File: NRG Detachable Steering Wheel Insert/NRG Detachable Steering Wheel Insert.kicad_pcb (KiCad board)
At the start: 2 copper layers, 34 x 34 mm, 18 parts, among them J1 Conn_01x01, J10 Conn_01x01, J11 Conn_01x01, J12 Conn_01x01, J13 Conn_01x01, J14 Conn_01x01, J15 Conn_01x01, J16 Conn_01x01, J2 Conn_01x01, J3 Conn_01x01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

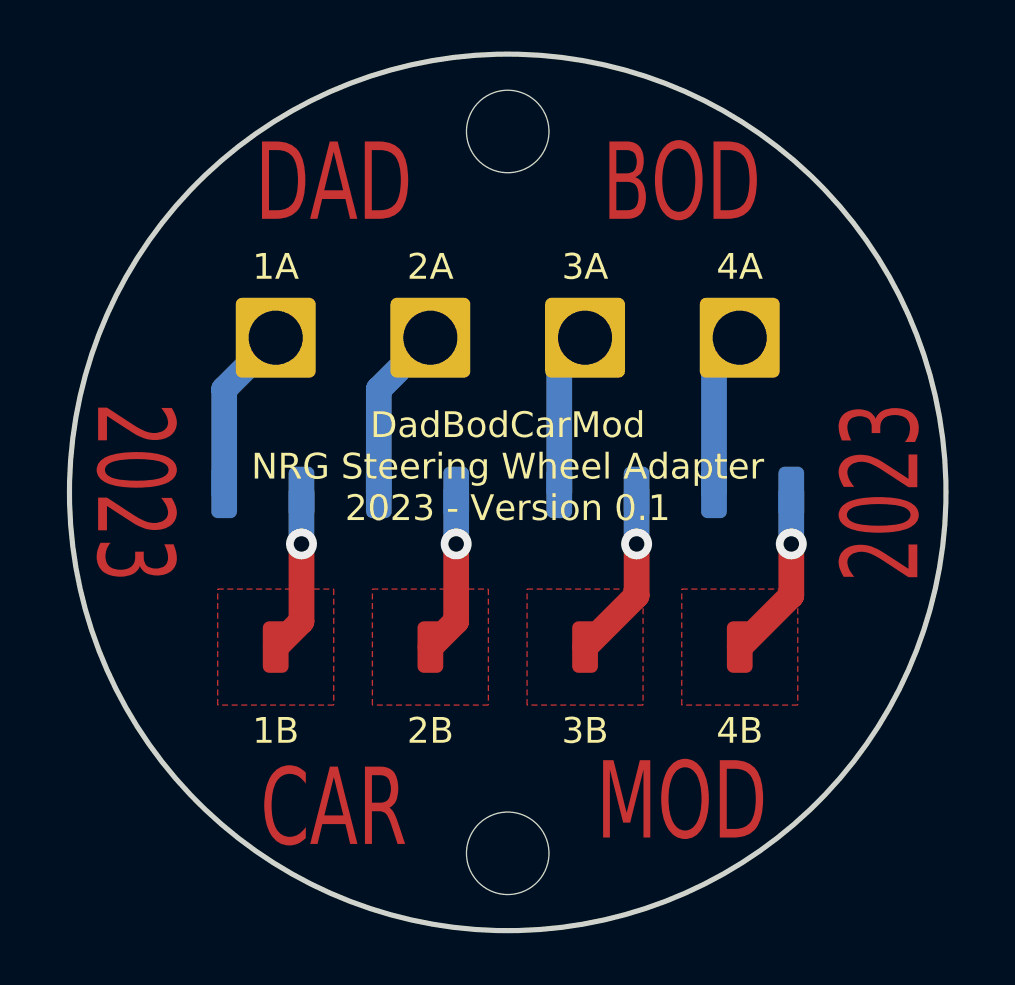
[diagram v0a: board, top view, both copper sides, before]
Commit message: Updating the steering wheel insert to not touch the metal of the steering wheel.
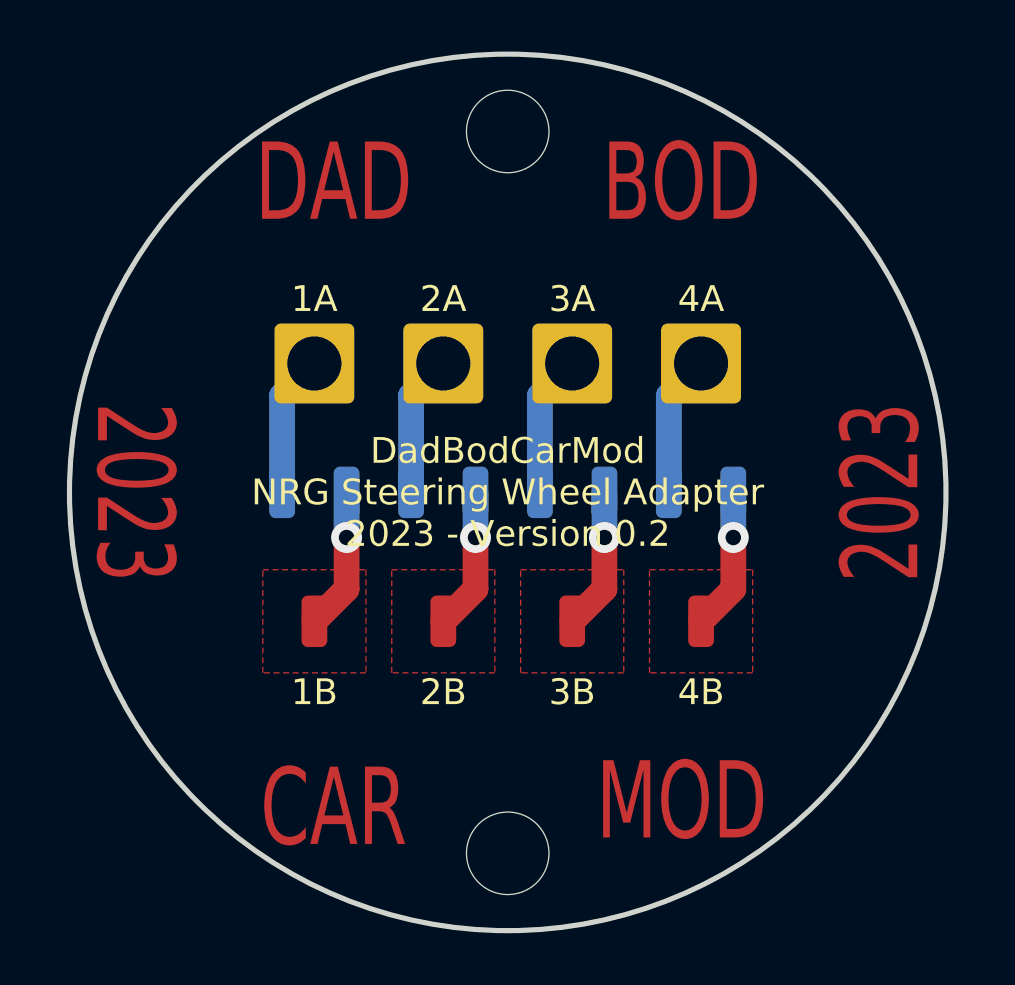
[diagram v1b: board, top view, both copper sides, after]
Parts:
- moved J16 2.25 mm to (78.8, 70.0)
- moved J5 2.25 mm to (61.2, 70.0)
- moved J1 1.80 mm to (62.5, 65.0)
- moved J12 1.80 mm to (77.5, 75.0)
- moved J4 1.80 mm to (77.5, 65.0)
- moved J9 1.80 mm to (62.5, 75.0)
- moved J13 1.75 mm to (63.8, 70.0)
- moved J8 1.75 mm to (76.2, 70.0)
- moved J15 1.25 mm to (73.8, 70.0)
- moved J6 1.25 mm to (66.2, 70.0)
- moved J10 1.12 mm to (67.5, 75.0)
- moved J11 1.12 mm to (72.5, 75.0)
- moved J2 1.12 mm to (67.5, 65.0)
- moved J3 1.12 mm to (72.5, 65.0)
- moved J14 0.75 mm to (68.8, 70.0)
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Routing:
- net Net-(J2-Pad1): track 6.83 -> 5.52 mm
- net Net-(J12-Pad1): track 6.83 -> 5.52 mm
- net Net-(J11-Pad1): track 6.83 -> 5.52 mm
- net Net-(J1-Pad1): track 6.83 -> 5.52 mm
- net Net-(J4-Pad1): track 6.41 -> 5.52 mm
- net Net-(J13-Pad1): track 6.41 -> 5.52 mm
- net Net-(J10-Pad1): track 6.41 -> 5.52 mm
- net Net-(J3-Pad1): track 6.41 -> 6.93 mm
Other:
- board text added: "DadBodCarMod NRG Steering Wheel Adapter 2023 - Version 0.2"
- board text removed: "DadBodCarMod NRG Steering Wheel Adapter 2023 - Version 0.1"
